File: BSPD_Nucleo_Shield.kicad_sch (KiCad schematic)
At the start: 35 parts, among them J1 Conn_01x03, J2 Conn_01x02, J3 Conn_01x02, J4 Digital/PWM, J5 Power, J6 Digital/PWM, J7 Analog, J8 Conn_01x03, Q1 IRFB4110, U1 LM2596S-ADJ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

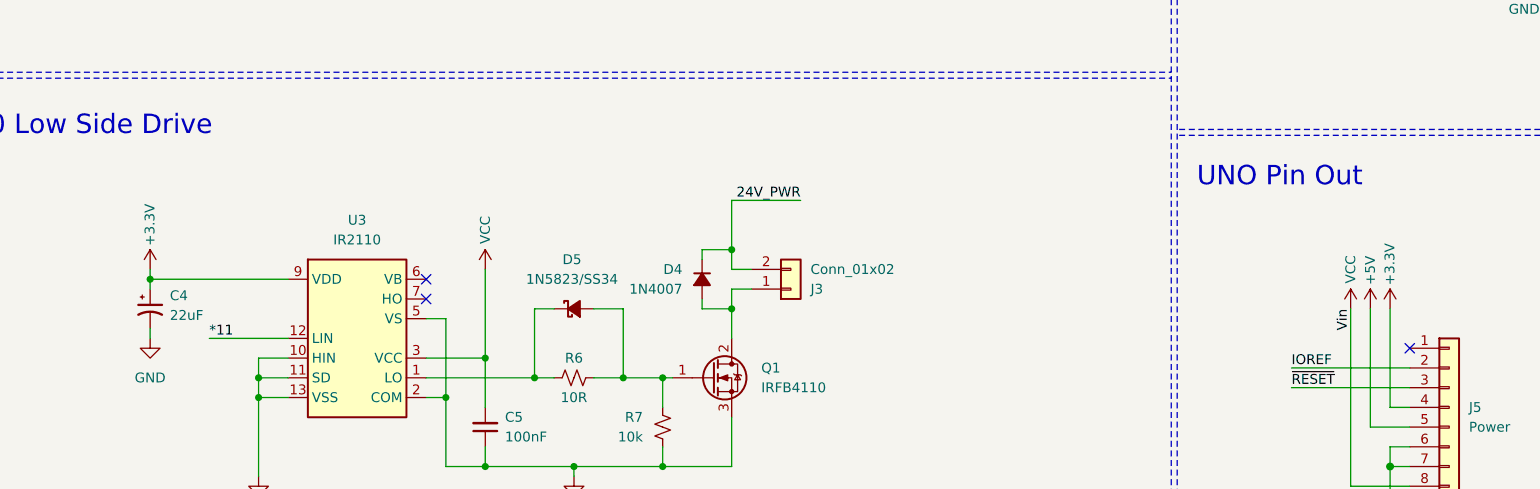
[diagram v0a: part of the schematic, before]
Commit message: updated to kicad8.0.1
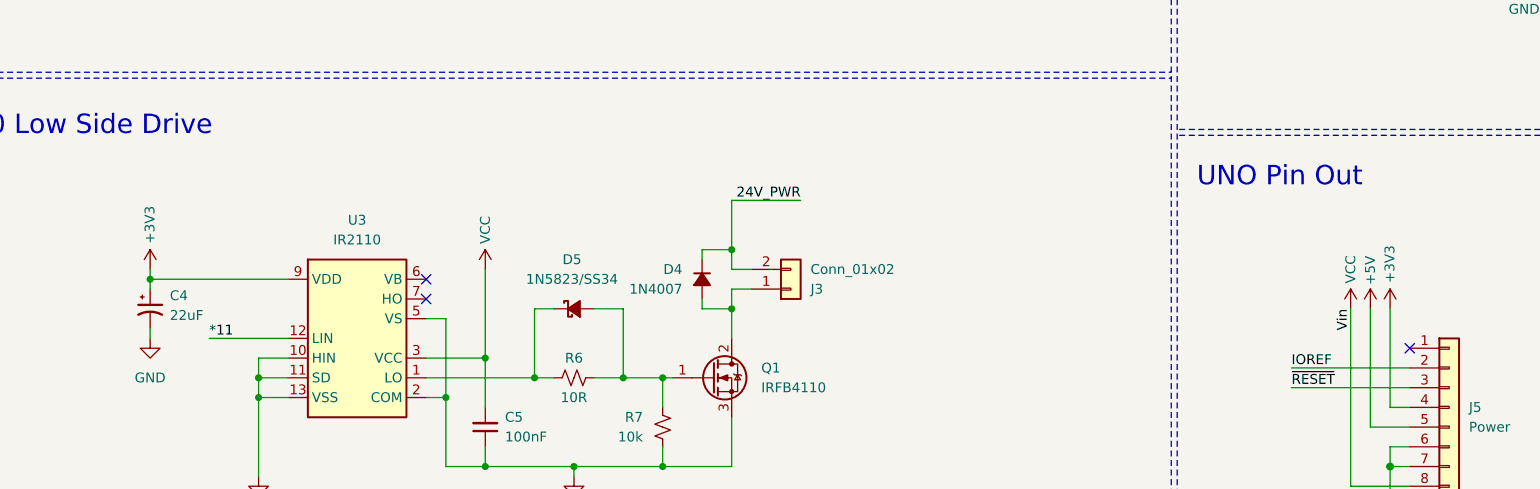
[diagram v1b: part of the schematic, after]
